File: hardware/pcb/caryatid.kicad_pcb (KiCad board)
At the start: 2 copper layers, 150 x 90 mm, 135 parts, among them J1 DC in, J10 FSR, J11 Digital bus, J12 RGB status, J13 Comms A - Qwiic, J14 Mic bias return, J15 Comms B - module, J16 Expansion / SPI1, J17 Audio out L/R/G, J18 Audio in L/R/rtn, J19 Comms A - module, J3 Latch switch, J4 Charge LEDs, J5 Analogue bus, J6 SW1 switch, J7 SW2 switch, J8 SW3 switch, J9 Soft pot, U1 BQ24074RGT, U2 TPS61023DRL, U3 74HC14, U4 MCP6002

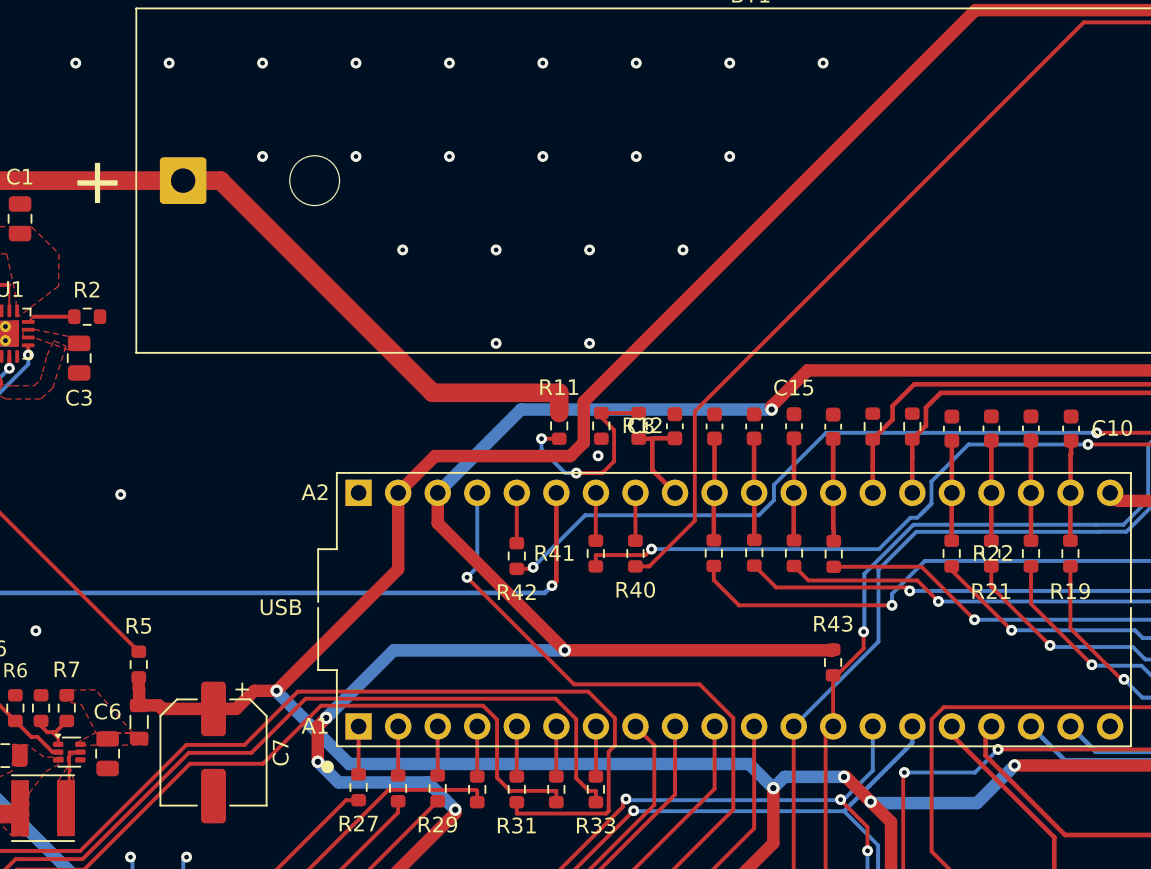
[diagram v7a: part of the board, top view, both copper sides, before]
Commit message: Stitch the orphaned ground islands; 4 -> 1, and the last one cannot be
  GND pour islands       4 -> 1
  floating GND copper  238 -> 7.5 mm2
  unconnected            4 -> 1
  track_dangling         1 -> 0
  clearance, parity      0, 0

--grid COULD NEVER FIX THESE, BY CONSTRUCTION. grid_stitch tests every
candidate with poly_contains(fmain, c) -- fmain being the LARGEST F.Cu
island -- so a point inside any other island is rejected before anything
else is weighed. An orphan is by definition not the largest, so the grid
skips exactly the copper that needs help. Running --grid and finding
islands left over was never a pitch problem; it was the wrong tool.

--islands places one via per orphan, at the point furthest from the
island edge so the annulus survives the refill, and still requires the
via to reach the MAIN B.Cu island -- a via landing in a stranded B.Cu
island joins one orphan to another and adds a hole for nothing.

  160.2 mm2 -> via (128.775, 38.300)   1.03 mm from the nearest edge
   47.3 mm2 -> via (136.677, 62.132)   0.75 mm
   23.1 mm2 -> via ( 75.488, 81.417)   1.19 mm

Also moved the island/grid computation ABOVE the dry-run return. --islands
previously did nothing without --apply, which is a bad shape for a tool
that writes copper.

THE RGB_G STUB WAS REDUNDANT COPPER, NOT A ROUTING ERROR. 0.956 mm from
(128.956, 64.294) to (128.280, 64.970), cross product 0.000000000 against
the segment that follows it from the same node -- a duplicate lying
exactly on top of the first 75% of it. Removed; track_dangling is 0 and
the connection never went through it.

THE LAST ISLAND CANNOT BE STITCHED, AND I WAS WRONG TWICE ABOUT WHY.

I said RGB_G carved the void under it. It does not: RGB_G sits at
x >= 128.96 and the void reaches x 124.76. I had inferred cause from a
scan that only caught tracks with an ENDPOINT in the region, and RGB_B
passes straight through without ending there.

I then said RGB_B was the culprit and proposed rerouting it. Tested
rather than as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
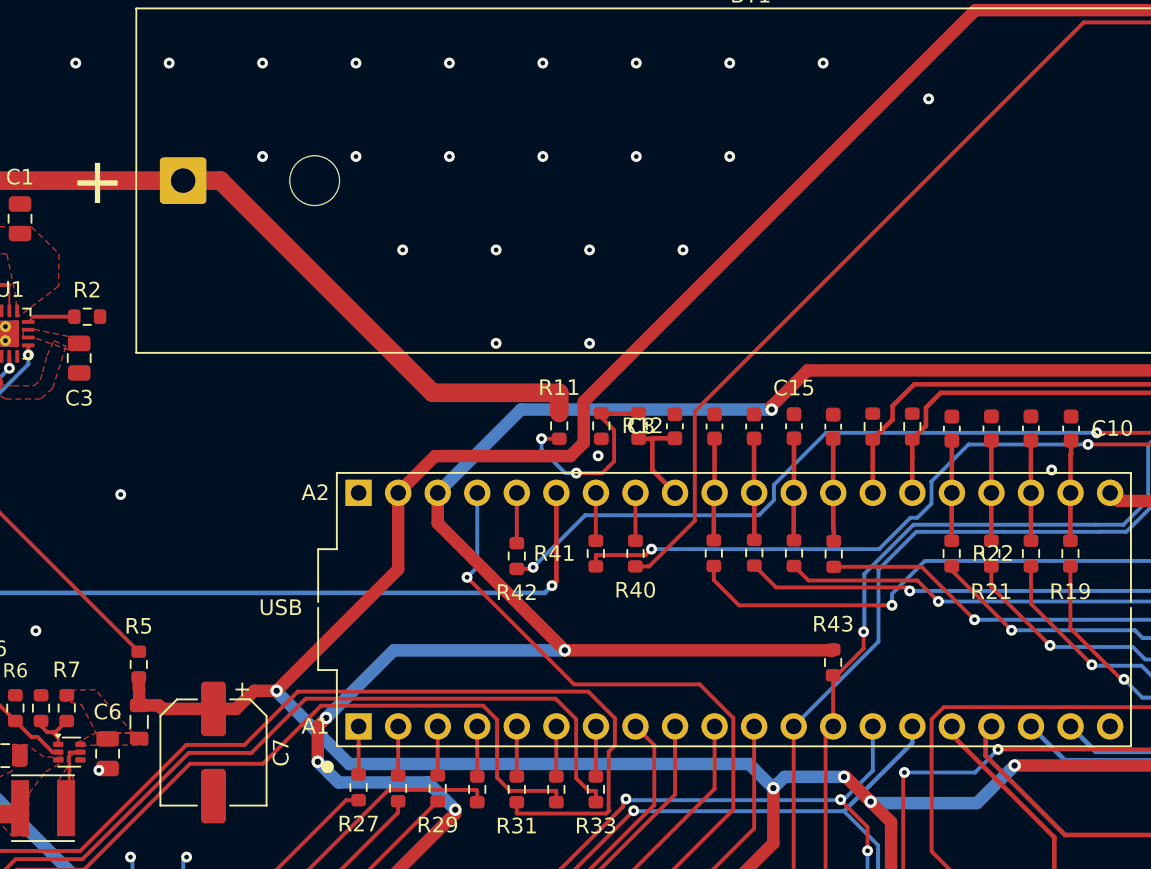
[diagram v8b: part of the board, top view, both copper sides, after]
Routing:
- net /panel-io/RGB_G: track 90.1 -> 89.2 mm
- net GND: vias 102 -> 105
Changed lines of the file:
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@@
 	)
 	(segment
-		(start 128.956 64.294)
-		(end 128.28 64.97)
-		(width 0.25)
-		(layer "B.Cu")
-		(net 34)
-	)
-	(segment
 		(start 139.01 60.491)
 		(end 131.339 60.491)
@@
 	)
 	(via
+		(at 128.7746 38.2995)
+		(size 0.7)
+		(drill 0.3)
+		(layers "F.Cu" "B.Cu")
+		(net 91)
+	)
+	(via
+		(at 75.488 81.4172)
+		(size 0.7)
+		(drill 0.3)
+		(layers "F.Cu" "B.Cu")
+		(net 91)
+	)
+	(via
 		(at 104 36)
 		(size 0.7)
@@
 		(size 0.7)
 		(drill 0.3)
+		(layers "F.Cu" "B.Cu")
+		(net 91)
+	)
+	(via
+		(at 136.6765 62.1315)
+		(size 0.7)
+		(drill 0.3)
